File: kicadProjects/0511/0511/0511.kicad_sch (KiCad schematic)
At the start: 103 parts, among them SW1 SW_Push, SW10 SW_Push, SW11 SW_Push, SW12 SW_Push, SW13 SW_Push, SW14 SW_Push, SW15 SW_Push, SW16 SW_Push, SW17 SW_Push, SW18 SW_Push, SW19 SW_Push, SW2 SW_Push, SW20 SW_Push, SW21 SW_Push, SW22 SW_Push, SW23 SW_Push, SW24 SW_Push, SW25 SW_Push, SW26 SW_Push, SW27 SW_Push, SW28 SW_Push, SW29 SW_Push, SW3 SW_Push, SW30 SW_Push, SW31 SW_Push, SW32 SW_Push, SW33 SW_Push, SW34 SW_Push, SW35 SW_Push, SW36 SW_Push, SW37 SW_Push, SW38 SW_Push, SW39 SW_Push, SW4 SW_Push, SW40 SW_Push, SW41 SW_Push, SW42 SW_Push, SW43 SW_Push, SW44 SW_Push, SW45 SW_Push, SW46 SW_Push, SW47 SW_Push, SW48 SW_Push, SW5 SW_Push, SW6 SW_Push, SW7 SW_Push, SW8 SW_Push, SW9 SW_Push, U1 UDA1334A_Breakout, U2 YAAJ_BlackPill, U3 MCP23017, U4 MCP23017, U5 MCP23017

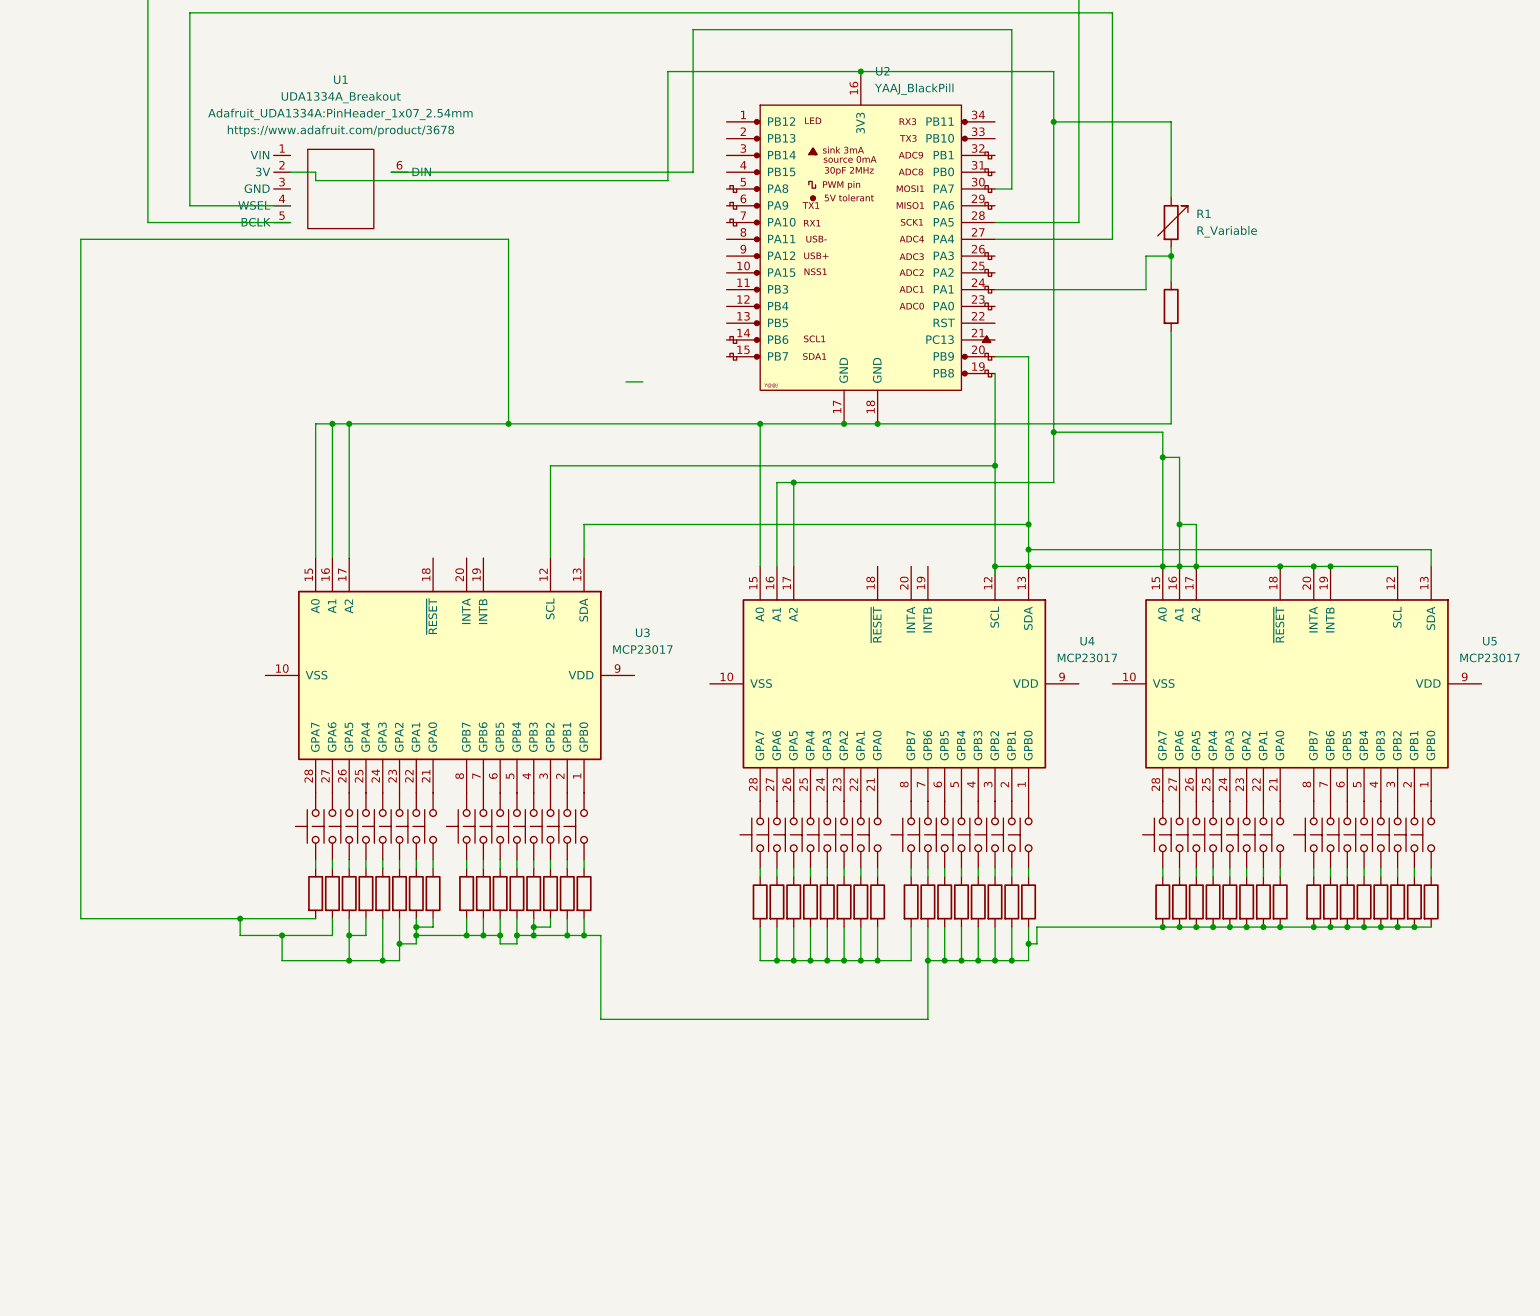
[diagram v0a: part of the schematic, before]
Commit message: ajout feuille hiérarchique
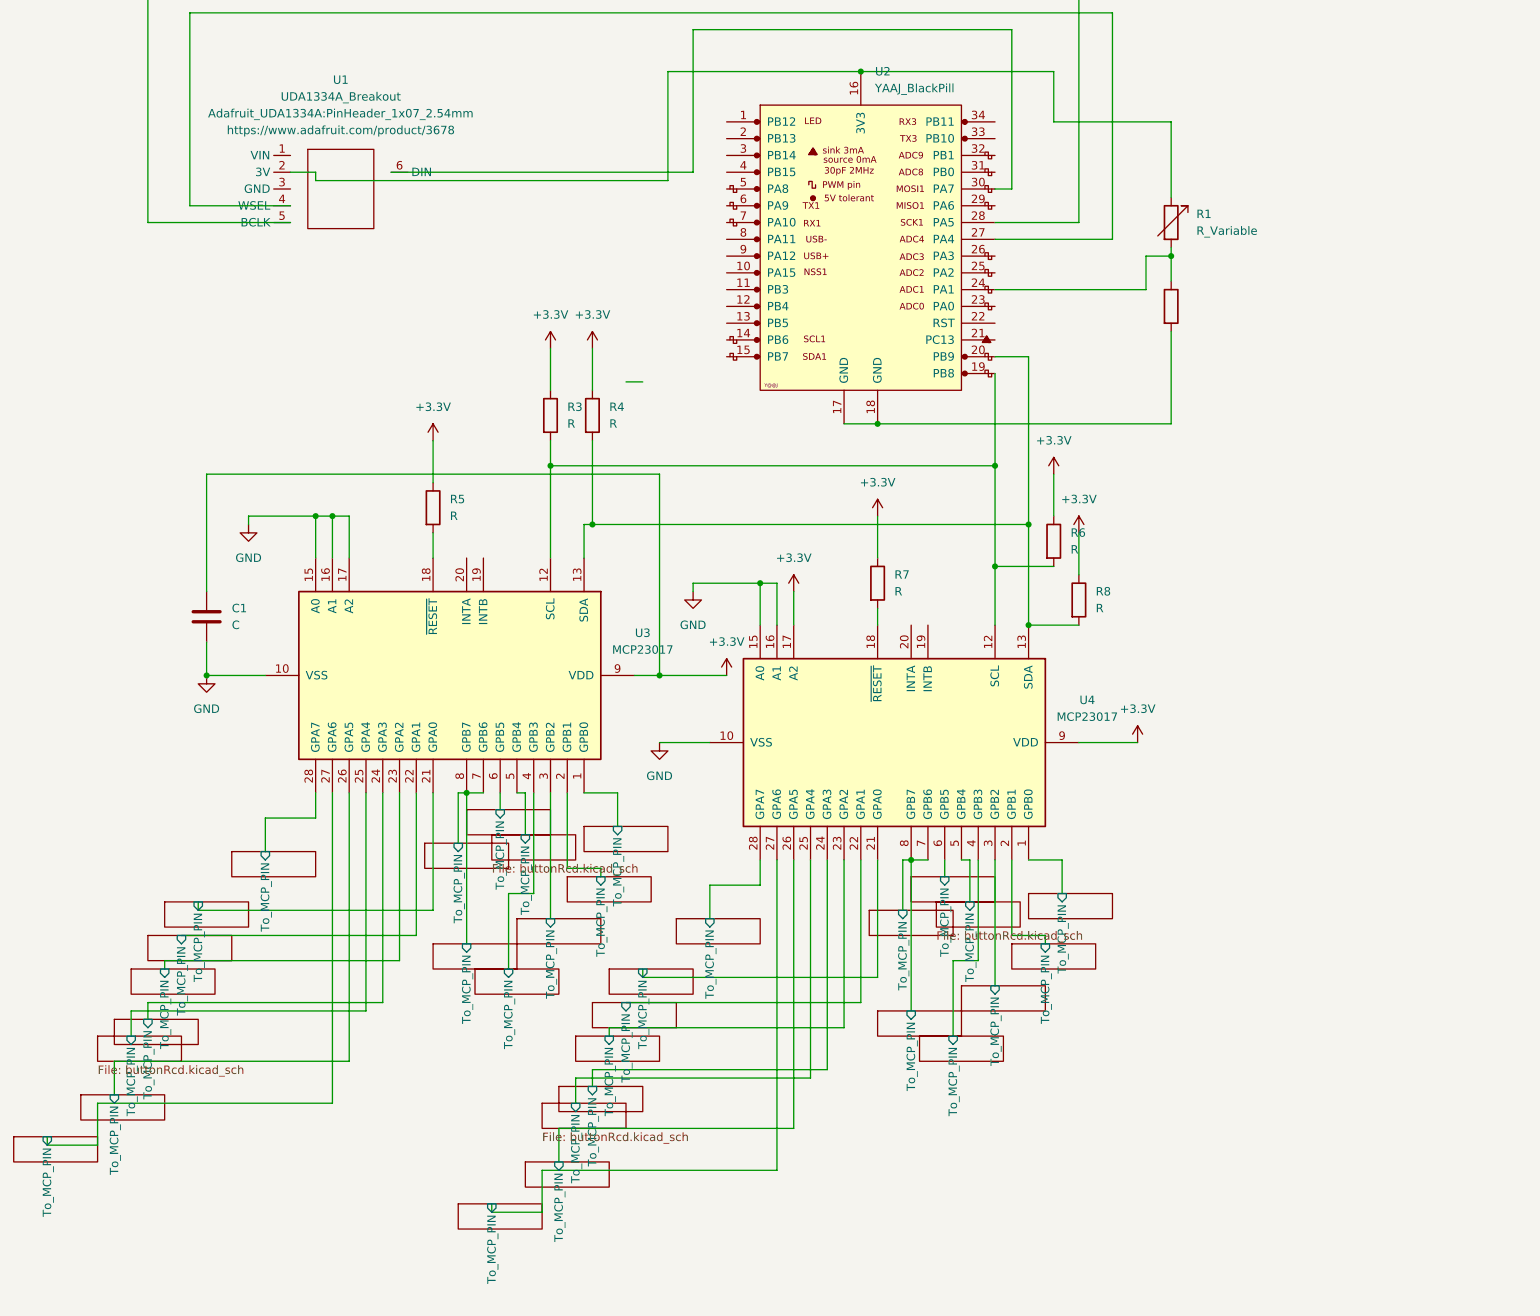
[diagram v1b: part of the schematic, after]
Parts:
- removed R10, R11, R12, R13, R14, R15, R16, R17, R18, R20, R21, R22, R23, R24, R25, R26, R27, R28, R29, R30, R31, R32, R33, R34, R36, R37, R38, R39, R40, R41, R42, R43, R44, R45, R46, R47, R48, R49, R50, R9: R, Resistor_THT:R_Axial_DIN0207_L6.3mm_D2.5mm_P7.62mm_Horizontal, symbol Device:R
- removed R19, R35: ~, Resistor_THT:R_Axial_DIN0207_L6.3mm_D2.5mm_P7.62mm_Horizontal, symbol Device:R
- removed SW1, SW10, SW11, SW12, SW13, SW14, SW15, SW16, SW17, SW18, SW19, SW2, SW20, SW21, SW22, SW23, SW24, SW25, SW26, SW27, SW28, SW29, SW3, SW30, SW31, SW32, SW33, SW34, SW35, SW36, SW37, SW38, SW39, SW4, SW40, SW41, SW42, SW43, SW44, SW45, SW46, SW47, SW48, SW5, SW6, SW7, SW8, SW9: SW_Push, Button_Switch_Keyboard:SW_Cherry_MX_1.00u_PCB, symbol Switch:SW_Push
- removed U5: MCP23017, Package_DIP:DIP-28_W7.62mm, symbol Stm32F411BlackPill:MCP23017
- added C1: C, symbol Device:C
- R3, R4: value 4.7k -> R; footprint Resistor_THT:R_Axial_DIN0207_L6.3mm_D2.5mm_P7.62mm_Horizontal -> (none)
- R5, R6, R7, R8: footprint Resistor_THT:R_Axial_DIN0207_L6.3mm_D2.5mm_P7.62mm_Horizontal -> (none)
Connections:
- net +3.3V: now reaches R3.1
- net +3.3V: now also R4.1, R5.1, R6.1, R7.1, R8.1, U3.9 (VDD), U4.17 (A2), U4.9 (VDD), C1.1
- net Button_RCD5/To_MCP_PIN: now reaches U3.22 (GPA1)
- net Button_RCD9/To_MCP_PIN: now reaches U3.5 (GPB4)
- net Button_RCD/To_MCP_PIN: now reaches U3.27 (GPA6)
- net Button_RCD26/To_MCP_PIN: now reaches U4.4 (GPB3)
- net Button_RCD19/To_MCP_PIN: now reaches U4.24 (GPA3)
- net Button_RCD28/To_MCP_PIN: now reaches U4.2 (GPB1)
- net Button_RCD13/To_MCP_PIN: now reaches U3.1 (GPB0)
- net Button_RCD21/To_MCP_PIN: now reaches U4.22 (GPA1)
- net Button_RCD23/To_MCP_PIN: now reaches U4.8 (GPB7)
- net Button_RCD23/To_MCP_PIN: now also U4.7 (GPB6)
- net Button_RCD15/To_MCP_PIN: now reaches U3.8 (GPB7)
- net Button_RCD15/To_MCP_PIN: now also U3.7 (GPB6)
- net Button_RCD17/To_MCP_PIN: now reaches U4.26 (GPA5)
- net Button_RCD24/To_MCP_PIN: now reaches U4.6 (GPB5)
- net Button_RCD1/To_MCP_PIN: now reaches U3.26 (GPA5)
- net Button_RCD18/To_MCP_PIN: now reaches U4.25 (GPA4)
- net Button_RCD27/To_MCP_PIN: now reaches U4.3 (GPB2)
- net Button_RCD2/To_MCP_PIN: now reaches U3.25 (GPA4)
- net Button_RCD11/To_MCP_PIN: now reaches U3.3 (GPB2)
- net Button_RCD20/To_MCP_PIN: now reaches U4.23 (GPA2)
- net Button_RCD22/To_MCP_PIN: now reaches U4.21 (GPA0)
- net Button_RCD12/To_MCP_PIN: now reaches U3.2 (GPB1)
- net Button_RCD29/To_MCP_PIN: now reaches U4.1 (GPB0)
- net GND: now reaches U4.10 (VSS)
- net GND: now also U3.10 (VSS), U3.15 (A0), U3.16 (A1), U3.17 (A2), U4.15 (A0), U4.16 (A1), C1.2
- net at U4.18 (~{RESET}): now also R7.2
- net Button_RCD16/To_MCP_PIN: now reaches U4.27 (GPA6)
- net Button_RCD30/To_MCP_PIN: now reaches U4.28 (GPA7)
- net Button_RCD25/To_MCP_PIN: now reaches U4.5 (GPB4)
- net at U3.18 (~{RESET}): now also R5.2
- net Button_RCD6/To_MCP_PIN: now reaches U3.21 (GPA0)
- net Button_RCD4/To_MCP_PIN: now reaches U3.23 (GPA2)
- net Button_RCD3/To_MCP_PIN: now reaches U3.24 (GPA3)
- net Button_RCD14/To_MCP_PIN: now reaches U3.28 (GPA7)
- net Button_RCD10/To_MCP_PIN: now reaches U3.4 (GPB3)
- net Button_RCD8/To_MCP_PIN: now reaches U3.6 (GPB5)
- new net: R4.2, R8.2, U2.20 (PB9), U3.13 (SDA), U4.13 (SDA)
- new net: R1.1, U1.2 (3V), U2.16 (3V3)
- new net: R3.2, R6.2, U2.19 (PB8), U3.12 (SCL), U4.12 (SCL)
- new net: R2.2, U2.17 (GND), U2.18 (GND)
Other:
- added sheet Button_RCD (buttonRcd.kicad_sch)
- added sheet Button_RCD1 (buttonRcd.kicad_sch)
- added sheet Button_RCD10 (buttonRcd.kicad_sch)
- added sheet Button_RCD11 (buttonRcd.kicad_sch)
- added sheet Button_RCD12 (buttonRcd.kicad_sch)
- added sheet Button_RCD13 (buttonRcd.kicad_sch)
- added sheet Button_RCD14 (buttonRcd.kicad_sch)
- added sheet Button_RCD15 (buttonRcd.kicad_sch)
- added sheet Button_RCD16 (buttonRcd.kicad_sch)
- added sheet Button_RCD17 (buttonRcd.kicad_sch)
- added sheet Button_RCD18 (buttonRcd.kicad_sch)
- added sheet Button_RCD19 (buttonRcd.kicad_sch)
- added sheet Button_RCD2 (buttonRcd.kicad_sch)
- added sheet Button_RCD20 (buttonRcd.kicad_sch)
- added sheet Button_RCD21 (buttonRcd.kicad_sch)
- added sheet Button_RCD22 (buttonRcd.kicad_sch)
- added sheet Button_RCD23 (buttonRcd.kicad_sch)
- added sheet Button_RCD24 (buttonRcd.kicad_sch)
- added sheet Button_RCD25 (buttonRcd.kicad_sch)
- added sheet Button_RCD26 (buttonRcd.kicad_sch)
- added sheet Button_RCD27 (buttonRcd.kicad_sch)
- added sheet Button_RCD28 (buttonRcd.kicad_sch)
- added sheet Button_RCD29 (buttonRcd.kicad_sch)
- added sheet Button_RCD3 (buttonRcd.kicad_sch)
- added sheet Button_RCD30 (buttonRcd.kicad_sch)
- added sheet Button_RCD31 (buttonRcd.kicad_sch)
- added sheet Button_RCD4 (buttonRcd.kicad_sch)
- added sheet Button_RCD5 (buttonRcd.kicad_sch)
- added sheet Button_RCD6 (buttonRcd.kicad_sch)
- added sheet Button_RCD7 (buttonRcd.kicad_sch)
- added sheet Button_RCD8 (buttonRcd.kicad_sch)
- added sheet Button_RCD9 (buttonRcd.kicad_sch)

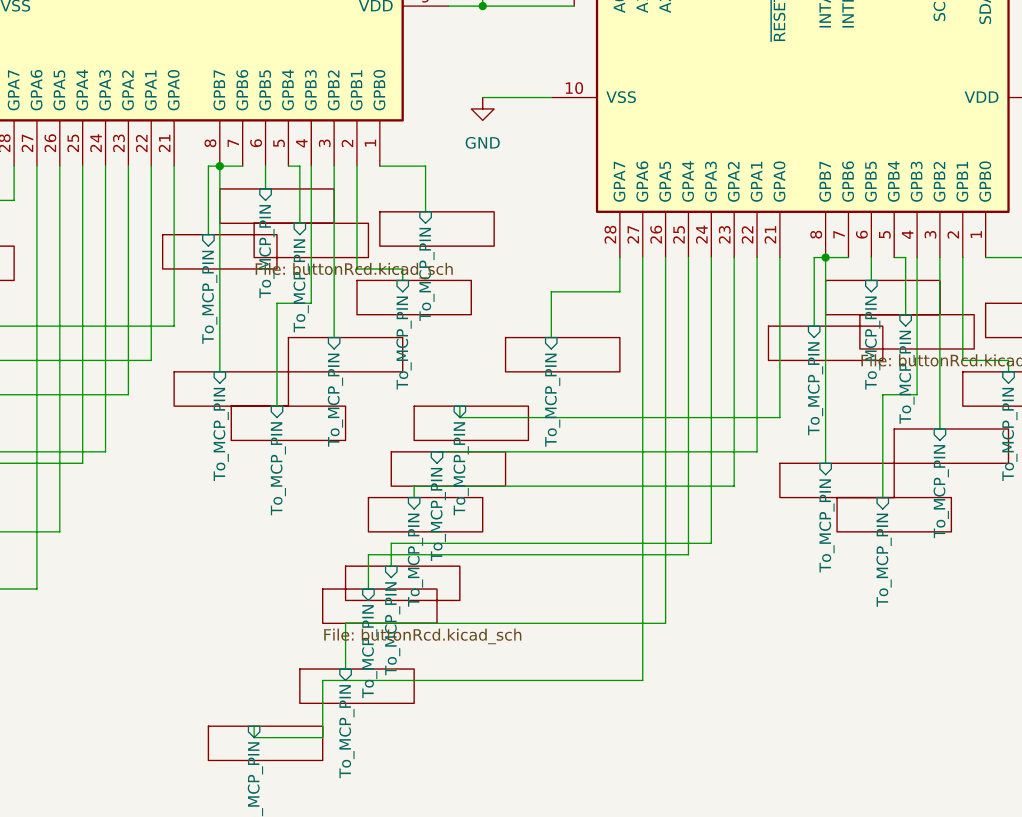
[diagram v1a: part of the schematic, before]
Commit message: correctifs connections mcp23017
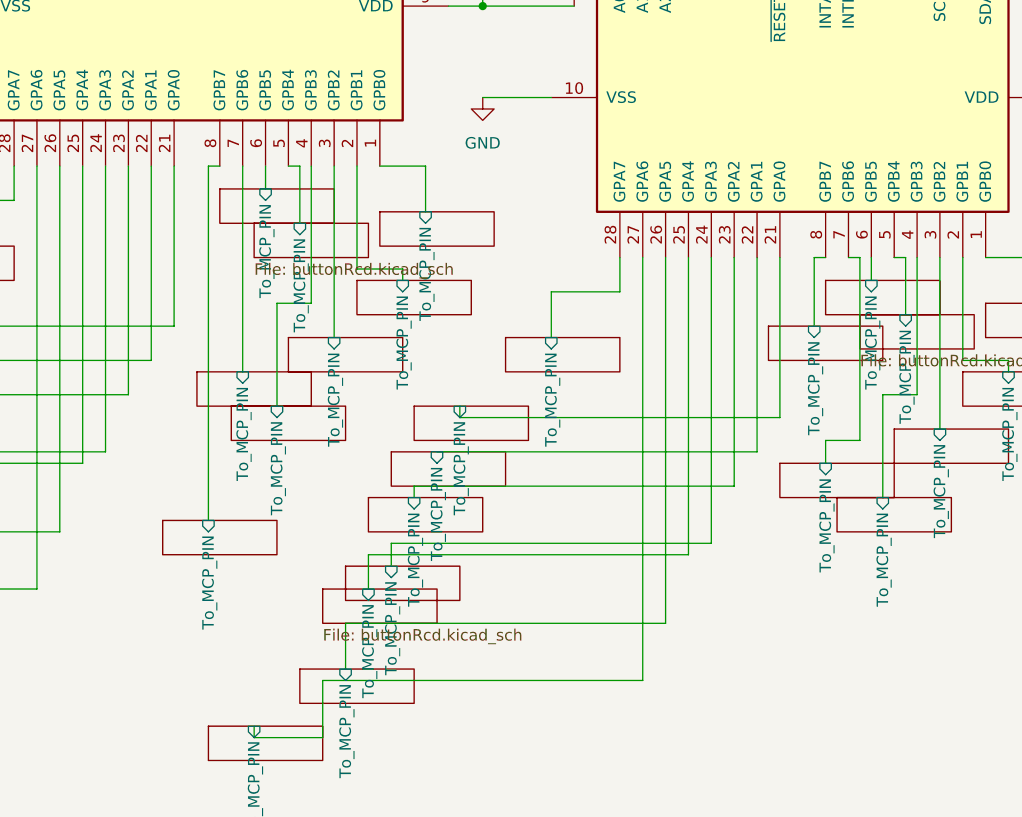
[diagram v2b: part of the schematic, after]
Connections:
- net Button_RCD15/To_MCP_PIN: no longer U3.8 (GPB7)
- net Button_RCD23/To_MCP_PIN: no longer U4.7 (GPB6)
- new net Button_RCD31/To_MCP_PIN: U4.7 (GPB6)
- new net Button_RCD7/To_MCP_PIN: U3.8 (GPB7)
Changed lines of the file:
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@@
 	)
 	(junction
-		(at 152.4 144.78)
-		(diameter 0)
-		(color 0 0 0 0)
-	)
-	(junction
 		(at 104.14 93.98)
 		(diameter 0)
@@
 	)
 	(junction
-		(at 85.09 134.62)
-		(diameter 0)
-		(color 0 0 0 0)
-	)
-	(junction
 		(at 64.77 92.71)
 		(diameter 0)
@@
 	(wire
 		(pts
-			(xy 21.59 187.96) (xy 29.21 187.96)
+			(xy 156.21 144.78) (xy 154.94 144.78)
 		)
 		(stroke
@@
 	(wire
 		(pts
-			(xy 101.6 177.8) (xy 101.6 181.61)
+			(xy 21.59 187.96) (xy 29.21 187.96)
 		)
 		(stroke
@@
 	(wire
 		(pts
-			(xy 74.93 134.62) (xy 74.93 160.02)
+			(xy 101.6 177.8) (xy 101.6 181.61)
 		)
 		(stroke
@@
 	(wire
 		(pts
-			(xy 101.6 177.8) (xy 137.16 177.8)
+			(xy 74.93 134.62) (xy 74.93 160.02)
 		)
 		(stroke
@@
 	(wire
 		(pts
-			(xy 29.21 181.61) (xy 64.77 181.61)
+			(xy 101.6 177.8) (xy 137.16 177.8)
 		)
 		(stroke
@@
 	(wire
 		(pts
-			(xy 85.09 134.62) (xy 87.63 134.62)
+			(xy 29.21 181.61) (xy 64.77 181.61)
 		)
 		(stroke
@@
 	(wire
 		(pts
+			(xy 151.13 144.78) (xy 151.13 152.4)
+		)
+		(stroke
+			(width 0)
+			(type default)
+		)
+	)
+	(wire
+		(pts
 			(xy 29.21 187.96) (xy 29.21 181.61)
 		)
@@
 	(wire
 		(pts
-			(xy 83.82 142.24) (xy 83.82 134.62)
-		)
-		(stroke
-			(width 0)
-			(type default)
-		)
-	)
-	(wire
-		(pts
 			(xy 167.64 43.18) (xy 165.1 43.18)
 		)
@@
 	(wire
 		(pts
-			(xy 83.82 134.62) (xy 85.09 134.62)
-		)
-		(stroke
-			(width 0)
-			(type default)
-		)
-	)
-	(wire
-		(pts
 			(xy 165.1 50.8) (xy 182.88 50.8)
 		)
@@
 	(wire
 		(pts
-			(xy 95.25 149.86) (xy 95.25 134.62)
+			(xy 87.63 134.62) (xy 87.63 157.48)
 		)
 		(stroke
@@
 	(wire
 		(pts
-			(xy 85.09 157.48) (xy 85.09 134.62)
+			(xy 95.25 149.86) (xy 95.25 134.62)
 		)
 		(stroke
@@
 	(wire
 		(pts
-			(xy 152.4 167.64) (xy 152.4 144.78)
+			(xy 152.4 165.1) (xy 156.21 165.1)
 		)
 		(stroke
@@
 	(wire
 		(pts
+			(xy 83.82 134.62) (xy 83.82 173.99)
+		)
+		(stroke
+			(width 0)
+			(type default)
+		)
+	)
+	(wire
+		(pts
+			(xy 156.21 165.1) (xy 156.21 144.78)
+		)
+		(stroke
+			(width 0)
+			(type default)
+		)
+	)
+	(wire
+		(pts
 			(xy 167.64 144.78) (xy 167.64 156.21)
 		)
@@
 	(wire
 		(pts
-			(xy 152.4 144.78) (xy 154.94 144.78)
+			(xy 152.4 167.64) (xy 152.4 165.1)
 		)
 		(stroke
@@
 	(wire
 		(pts
-			(xy 151.13 152.4) (xy 151.13 144.78)
+			(xy 83.82 134.62) (xy 85.09 134.62)
 		)
 		(stroke
@@
 	)
 	(sheet
-		(at 78.74 142.24)
+		(at 78.74 173.99)
 		(size 12.7 3.81)
 		(exclude_from_sim no)
@@
 		)
 		(property "Sheetname" "Button_RCD7"
-			(at 78.74 141.5284 0)
+			(at 78.74 173.2784 0)
 			(effects
 				(font
@@
 		)
 		(property "Sheetfile" "buttonRcd.kicad_sch"
-			(at 78.74 146.6346 0)
+			(at 78.74 178.3846 0)
 			(effects
 				(font
@@
 		)
 		(pin "To_MCP_PIN" input
-			(at 83.82 142.24 90)
+			(at 83.82 173.99 90)
 			(effects
 				(font
@@
 	)
 	(sheet
-		(at 80.01 157.48)
+		(at 82.55 157.48)
 		(size 12.7 3.81)
 		(exclude_from_sim no)
@@
 		)
 		(property "Sheetname" "Button_RCD15"
-			(at 80.01 156.7684 0)
+			(at 82.55 156.7684 0)
 			(do_not_autoplace yes)
 			(effects
@@
 		)
 		(property "Sheetfile" "buttonRcd.kicad_sch"
-			(at 80.01 161.8746 0)
+			(at 82.55 161.8746 0)
 			(effects
 				(font
@@
 		)
 		(pin "To_MCP_PIN" input
-			(at 85.09 157.48 90)
+			(at 87.63 157.48 90)
 			(effects
 				(font
